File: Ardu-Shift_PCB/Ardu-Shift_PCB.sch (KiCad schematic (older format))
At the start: 16 parts, among them U1 OLED(SPI), U2 Arduino_Pro_Micro

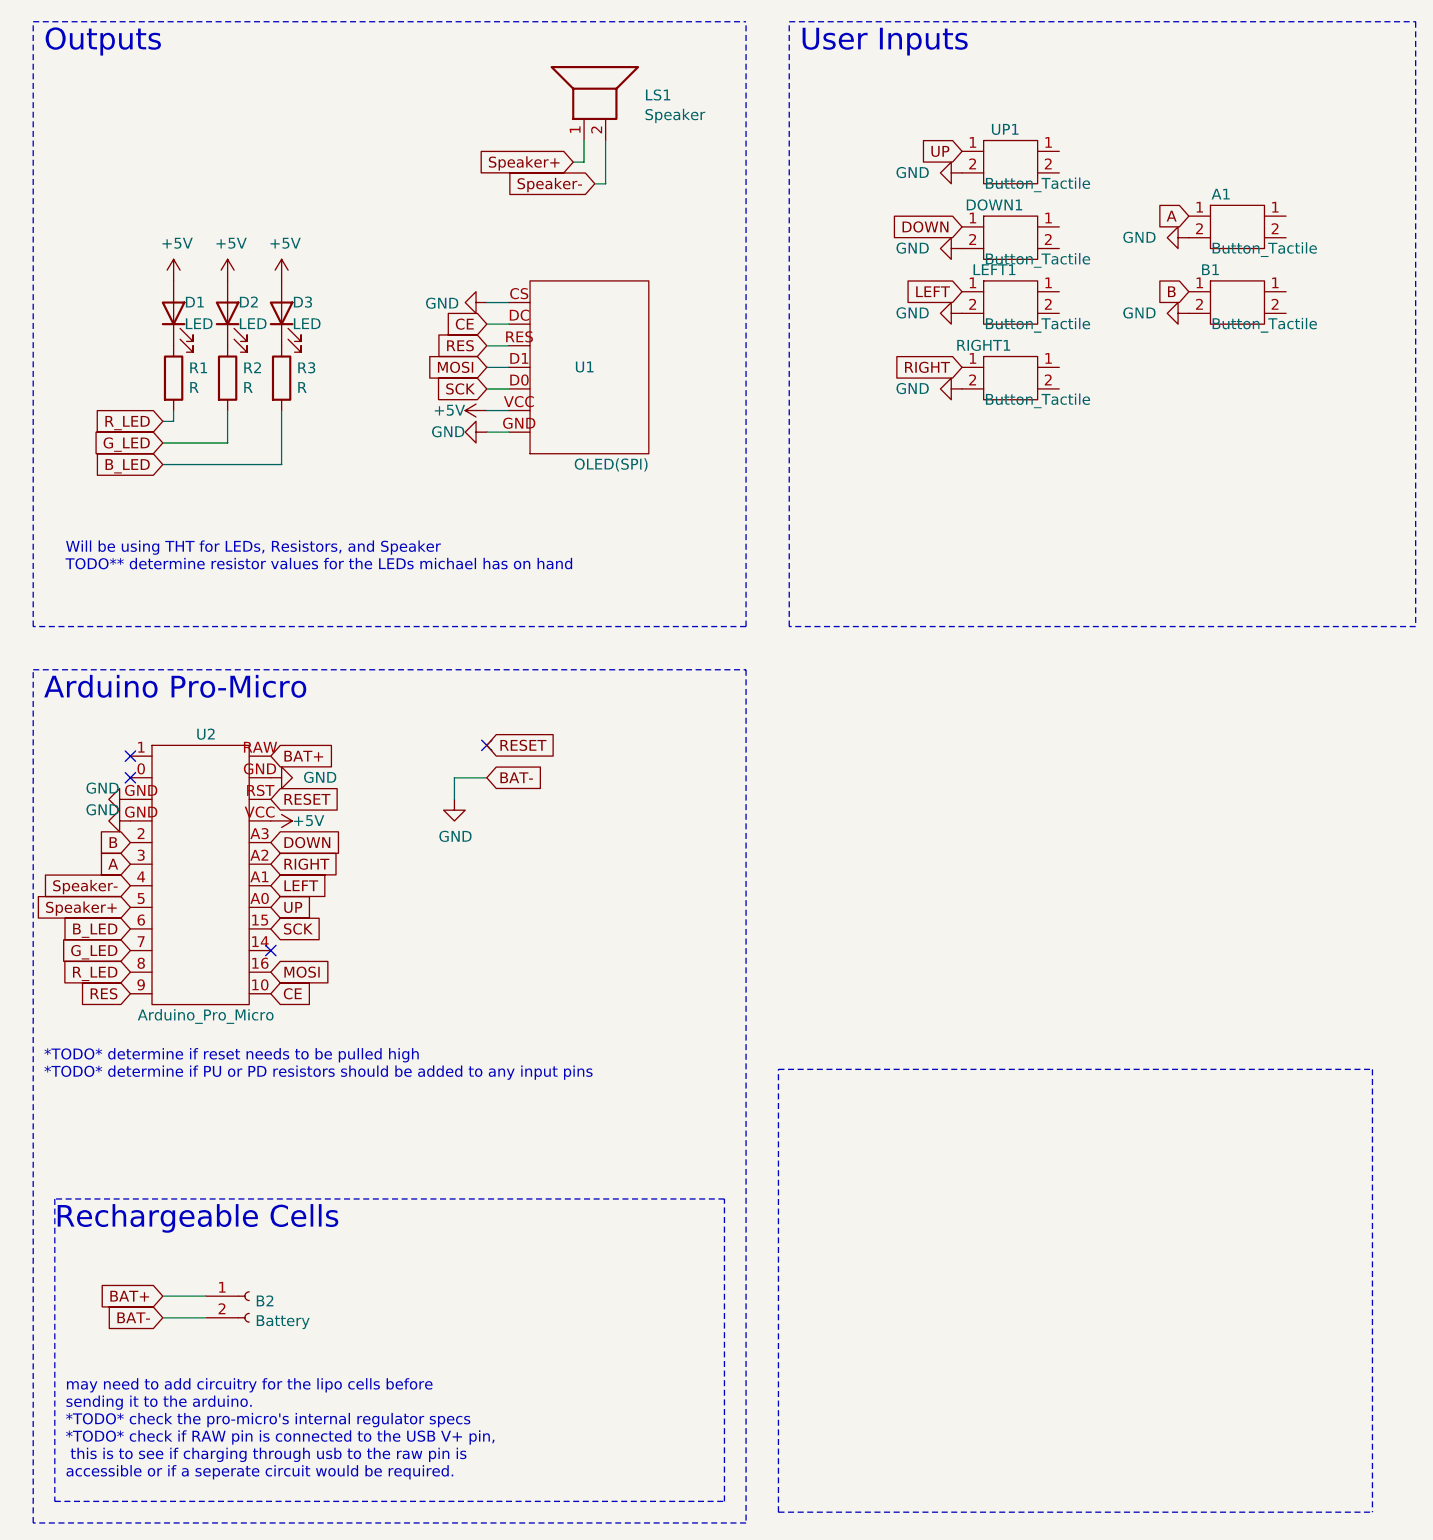
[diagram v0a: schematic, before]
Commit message: first version of the final assembly/routing of game-device PCB
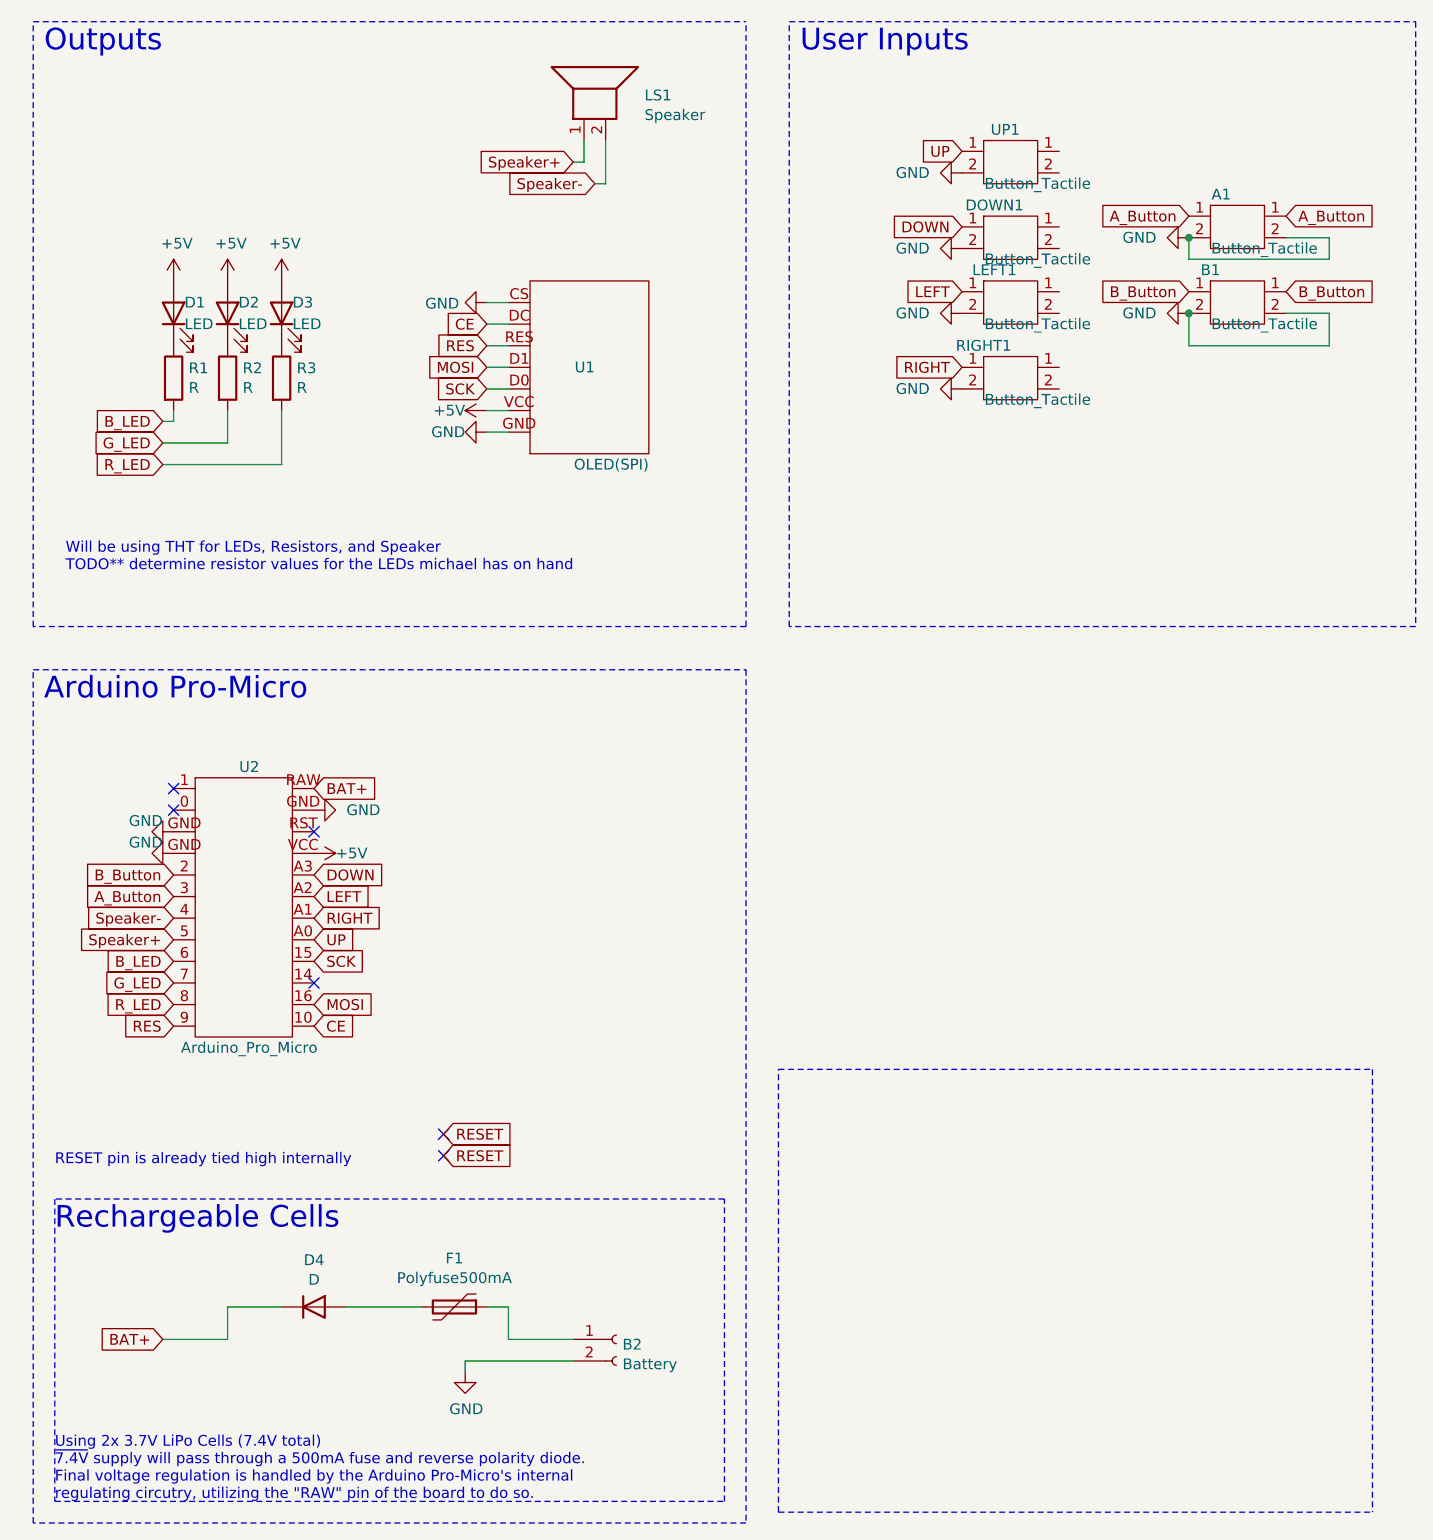
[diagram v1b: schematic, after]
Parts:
- added D4: D, Diode_THT:D_A-405_P10.16mm_Horizontal, symbol Device:D
- added F1: Polyfuse500mA, Resistor_THT:R_Axial_DIN0207_L6.3mm_D2.5mm_P7.62mm_Horizontal, symbol Device:Polyfuse
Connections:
- net A is gone; now on net A_Button: A1.1, U2.3
- net B is gone; now on net B_Button: B1.1, U2.2
- net BAT+: now also D4.1 (K); no longer B2.1 (Pin_1)
- net B_LED: now also R1.2; no longer R3.2
- net LEFT: now also U2.A2; no longer U2.A1
- net RESET: no longer U2.RST
- net RIGHT: now also U2.A1; no longer U2.A2
- net R_LED: now also R3.2; no longer R1.2
- net A_Button: now reaches A1.1
- net B_Button: now reaches B1.1
- new net: B2.1 (Pin_1), F1.1
- new net: D4.2 (A), F1.2
- no-connect marks 4 -> 6
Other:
- note added: "RESET pin is already tied high internally\n"
- note added: "Using 2x 3.7V LiPo Cells (7.4V total)\n~7.4V supply will pass through a 500mA fuse and reverse polarity diode.\nFinal voltage regulation is handled by the Arduino Pro-Micro's internal \nregulating circutry, utilizing the "RAW" pin of the board to do so."
- note removed: "*TODO* determine if reset needs to be pulled high\n*TODO* determine if PU or PD resistors should be added to any input pins"
- note removed: "may need to add circuitry for the lipo cells before \nsending it to the arduino. \n*TODO* check the pro-micro's internal regulator specs\n*TODO* check if RAW pin is connected to the USB V+ pin,\n this is to see if charging through usb to the raw pin is \naccessible or if a seperate circuit would be required.\n"
- moved on the sheet: B2, U2
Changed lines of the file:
@@
 	0    -1   -1   0
 $EndComp
-NoConn ~ 1100 4050
-NoConn ~ 1100 4150
+NoConn ~ 1300 4200
+NoConn ~ 1300 4300
 Text GLabel 3150 1300 0    50   Input ~ 0
 Speaker+
@@
 	1    0    0    -1
 $EndComp
-Text GLabel 1250 2500 0    50   Input ~ 0
+Text GLabel 1250 2700 0    50   Input ~ 0
 R_LED
 Text GLabel 1250 2600 0    50   Input ~ 0
 G_LED
-Text GLabel 1250 2700 0    50   Input ~ 0
+Text GLabel 1250 2500 0    50   Input ~ 0
 B_LED
 Wire Wire Line
@@
 Wire Wire Line
 	1250 2700 1800 2700
-Text GLabel 1100 5050 0    50   Input ~ 0
+Text GLabel 1300 5200 0    50   Input ~ 0
 R_LED
-Text GLabel 1100 4950 0    50   Input ~ 0
+Text GLabel 1300 5100 0    50   Input ~ 0
 G_LED
 $Comp
 L power:GND #PWR0104
 U 1 1 602F2938
-P 1100 4250
-F 0 "#PWR0104" H 1100 4000 50  0001 C CNN
-F 1 "GND" V 1050 4200 50  0000 R CNN
-F 2 "" H 1100 4250 50  0001 C CNN
-F 3 "" H 1100 4250 50  0001 C CNN
-	1    1100 4250
+P 1300 4400
+F 0 "#PWR0104" H 1300 4150 50  0001 C CNN
+F 1 "GND" V 1250 4350 50  0000 R CNN
+F 2 "" H 1300 4400 50  0001 C CNN
+F 3 "" H 1300 4400 50  0001 C CNN
+	1    1300 4400
 	0    1    1    0
 $EndComp
@@
 L power:GND #PWR0106
 U 1 1 602F760D
-P 1750 4150
-F 0 "#PWR0106" H 1750 3900 50  0001 C CNN
-F 1 "GND" V 1750 4000 50  0000 R CNN
-F 2 "" H 1750 4150 50  0001 C CNN
-F 3 "" H 1750 4150 50  0001 C CNN
-	1    1750 4150
+P 1950 4300
+F 0 "#PWR0106" H 1950 4050 50  0001 C CNN
+F 1 "GND" V 1950 4150 50  0000 R CNN
+F 2 "" H 1950 4300 50  0001 C CNN
+F 3 "" H 1950 4300 50  0001 C CNN
+	1    1950 4300
 	0    -1   -1   0
 $EndComp
 Text GLabel 2750 2250 0    50   Input ~ 0
 MOSI
-Text GLabel 1750 5050 2    50   Input ~ 0
+Text GLabel 1950 5200 2    50   Input ~ 0
 MOSI
 Text GLabel 2750 2050 0    50   Input ~ 0
 CE
-Text GLabel 1750 5150 2    50   Input ~ 0
+Text GLabel 1950 5300 2    50   Input ~ 0
 CE
 $Comp
@@
 Text GLabel 2750 2150 0    50   Input ~ 0
 RES
-Text GLabel 1100 5150 0    50   Input ~ 0
+Text GLabel 1300 5300 0    50   Input ~ 0
 RES
-Text GLabel 1750 4250 2    50   Input ~ 0
+Text GLabel 2550 5900 2    50   Input ~ 0
 RESET
-Text GLabel 1100 4850 0    50   Input ~ 0
+Text GLabel 1300 5000 0    50   Input ~ 0
 B_LED
-Text GLabel 1750 4750 2    50   Input ~ 0
+Text GLabel 1950 4900 2    50   Input ~ 0
 UP
-Text GLabel 1750 4450 2    50   Input ~ 0
+Text GLabel 1950 4600 2    50   Input ~ 0
 DOWN
-Text GLabel 1750 4550 2    50   Input ~ 0
+Text GLabel 1950 4800 2    50   Input ~ 0
 RIGHT
-Text GLabel 1750 4650 2    50   Input ~ 0
+Text GLabel 1950 4700 2    50   Input ~ 0
 LEFT
-Text GLabel 1750 4850 2    50   Input ~ 0
+Text GLabel 1950 5000 2    50   Input ~ 0
 SCK
 Text GLabel 2750 2350 0    50   Input ~ 0
 SCK
-NoConn ~ 1750 4950
+NoConn ~ 1950 5100
 $Comp
 L power:GND #PWR0109
@@
 $EndComp
 Text GLabel 6000 1900 0    50   Input ~ 0
-B
+B_Button
 Text GLabel 6000 1550 0    50   Input ~ 0
-A
+A_Button
 $Comp
 L Device:Button_Tactile B1
@@
 	1    0    0    -1
 $EndComp
-Text GLabel 2750 4000 2    50   Input ~ 0
+Text GLabel 2550 5800 2    50   Input ~ 0
 RESET
 Wire Notes Line
@@
 Text Notes 4200 800  0    100  ~ 0
 User Inputs\n
-Text GLabel 1250 6550 0    50   Input ~ 0
+Text GLabel 1250 6750 0    50   Input ~ 0
 BAT+
 Wire Notes Line
@@
 Text Notes 750  6250 0    100  ~ 0
 Rechargeable Cells\n
-Text GLabel 1750 4050 2    50   Input ~ 0
+Text GLabel 1950 4200 2    50   Input ~ 0
 BAT+
 Wire Notes Line
@@
 Wire Notes Line
 	3850 6100 750  6100
-Text GLabel 1250 6650 0    50   Input ~ 0
-BAT-
-Text GLabel 2750 4150 2    50   Input ~ 0
-BAT-
 $Comp
 L Connector:Conn_01x02_Female B2
 U 1 1 603C890C
-P 1650 6550
-F 0 "B2" H 1678 6526 50  0000 L CNN
-F 1 "Battery" H 1678 6435 50  0000 L CNN
-F 2 "Connector_PinHeader_2.54mm:PinHeader_1x02_P2.54mm_Vertical" H 1650 6550 50  0001 C CNN
-F 3 "~" H 1650 6550 50  0001 C CNN
-	1    1650 6550
-	1    0    0    -1
-$EndComp
-Wire Wire Line
-	1250 6650 1450 6650
-Wire Wire Line
-	1250 6550 1450 6550
-$Comp
-L power:GND #PWR0116
-U 1 1 603CB5E7
-P 2600 4250
-F 0 "#PWR0116" H 2600 4000 50  0001 C CNN
-F 1 "GND" H 2605 4077 50  0000 C CNN
-F 2 "" H 2600 4250 50  0001 C CNN
-F 3 "" H 2600 4250 50  0001 C CNN
-	1    2600 4250
-	1    0    0    -1
-$EndComp
-Wire Wire Line
-	2600 4250 2600 4150
-Wire Wire Line
-	2600 4150 2750 4150
-NoConn ~ 2750 4000
+P 3350 6750
+F 0 "B2" H 3378 6726 50  0000 L CNN
+F 1 "Battery" H 3378 6635 50  0000 L CNN
+F 2 "Connector_PinHeader_2.54mm:PinHeader_1x02_P2.54mm_Vertical" H 3350 6750 50  0001 C CNN
+F 3 "~" H 3350 6750 50  0001 C CNN
+	1    3350 6750
+	1    0    0    -1
+$EndComp
+NoConn ~ 2550 5800
 $Comp
 L power:GND #PWR0117
 U 1 1 603CE810
-P 1100 4350
-F 0 "#PWR0117" H 1100 4100 50  0001 C CNN
-F 1 "GND" V 1050 4300 50  0000 R CNN
-F 2 "" H 1100 4350 50  0001 C CNN
-F 3 "" H 1100 4350 50  0001 C CNN
-	1    1100 4350
+P 1300 4500
+F 0 "#PWR0117" H 1300 4250 50  0001 C CNN
+F 1 "GND" V 1250 4450 50  0000 R CNN
+F 2 "" H 1300 4500 50  0001 C CNN
+F 3 "" H 1300 4500 50  0001 C CNN
+	1    1300 4500
 	0    1    1    0
 $EndComp
@@
 Wire Notes Line
 	3950 3650 3950 7600
-Text Notes 800  7400 0    50   ~ 0
-may need to add circuitry for the lipo cells before \nsending it to the arduino. \n*TODO* check the pro-micro's internal regulator specs\n*TODO* check if RAW pin is connected to the USB V+ pin,\n this is to see if charging through usb to the raw pin is \naccessible or if a seperate circuit would be required.\n
+Text Notes 750  7500 0    50   ~ 0
+Using 2x 3.7V LiPo Cells (7.4V total)\n~7.4V supply will pass through a 500mA fuse and reverse polarity diode.\nFinal voltage regulation is handled by the Arduino Pro-Micro's internal \nregulating circutry, utilizing the "RAW" pin of the board to do so.
 Text Notes 800  3200 0    50   ~ 0
 Will be using THT for LEDs, Resistors, and Speaker \nTODO** determine resistor values for the LEDs michael has on hand\n
-Text Notes 700  5550 0    50   ~ 0
-*TODO* determine if reset needs to be pulled high\n*TODO* determine if PU or PD resistors should be added to any input pins
-Text GLabel 1100 4450 0    50   Input ~ 0
-B
-Text GLabel 1100 4550 0    50   Input ~ 0
-A
+Text Notes 750  5950 0    50   ~ 0
+RESET pin is already tied high internally\n
+Text GLabel 1300 4600 0    50   Input ~ 0
+B_Button
+Text GLabel 1300 4700 0    50   Input ~ 0
+A_Button
 $Comp
 L power:+5V #PWR0105
 U 1 1 602F42C8
-P 1750 4350
-F 0 "#PWR0105" H 1750 4200 50  0001 C CNN
-F 1 "+5V" V 1750 4450 50  0000 L CNN
-F 2 "" H 1750 4350 50  0001 C CNN
-F 3 "" H 1750 4350 50  0001 C CNN
-	1    1750 4350
-	0    1    1    0
-$EndComp
-Text GLabel 1100 4650 0    50   Input ~ 0
+P 1950 4500
+F 0 "#PWR0105" H 1950 4350 50  0001 C CNN
+F 1 "+5V" V 1950 4600 50  0000 L CNN
+F 2 "" H 1950 4500 50  0001 C CNN
+F 3 "" H 1950 4500 50  0001 C CNN
+	1    1950 4500
+	0    1    1    0
+$EndComp
+Text GLabel 1300 4800 0    50   Input ~ 0
 Speaker-
-Text GLabel 1100 4750 0    50   Input ~ 0
+Text GLabel 1300 4900 0    50   Input ~ 0
 Speaker+
 $Comp
 L Device:Arduino_Pro_Micro U2
 U 1 1 602C193C
-P 1450 4050
-F 0 "U2" H 1450 4150 50  0000 C CNN
-F 1 "Arduino_Pro_Micro" H 1450 2850 50  0000 C CNN
-F 2 "Module:Arduino_Pro_Micro" H 450 3500 50  0001 C CNN
-F 3 "" H 450 3500 50  0001 C CNN
-	1    1450 4050
-	1    0    0    -1
-$EndComp
+P 1650 4200
+F 0 "U2" H 1650 4300 50  0000 C CNN
+F 1 "Arduino_Pro_Micro" H 1650 3000 50  0000 C CNN
+F 2 "Module:Arduino_Pro_Micro" H 650 3650 50  0001 C CNN
+F 3 "" H 650 3650 50  0001 C CNN
+	1    1650 4200
+	1    0    0    -1
+$EndComp
+$Comp
+L Device:Polyfuse F1
+U 1 1 6044FB48
+P 2600 6600
+F 0 "F1" V 2375 6600 50  0000 C CNN
+F 1 "Polyfuse500mA" V 2466 6600 50  0000 C CNN
+F 2 "Resistor_THT:R_Axial_DIN0207_L6.3mm_D2.5mm_P7.62mm_Horizontal" H 2650 6400 50  0001 L CNN
+F 3 "~" H 2600 6600 50  0001 C CNN
+	1    2600 6600
+	0    1    1    0
+$EndComp
+Wire Wire Line
+	2750 6600 2850 6600
+Wire Wire Line
+	2850 6600 2850 6750
+Wire Wire Line
+	2850 6750 3150 6750
+$Comp
+L Device:D D4
+U 1 1 604552AC
+P 1950 6600
+F 0 "D4" H 1950 6817 50  0000 C CNN
+F 1 "D" H 1950 6726 50  0000 C CNN
+F 2 "Diode_THT:D_A-405_P10.16mm_Horizontal" H 1950 6600 50  0001 C CNN
+F 3 "~" H 1950 6600 50  0001 C CNN
+	1    1950 6600
+	1    0    0    -1
+$EndComp
+Wire Wire Line
+	1800 6600 1550 6600
+Wire Wire Line
+	1550 6600 1550 6750
+Wire Wire Line
+	1250 6750 1550 6750
+Wire Wire Line
+	2100 6600 2450 6600
+NoConn ~ 2550 5900
+NoConn ~ 1950 4400
+$Comp
+L power:GND #PWR0116
+U 1 1 6048AF00
+P 2650 6900
+F 0 "#PWR0116" H 2650 6650 50  0001 C CNN
+F 1 "GND" H 2655 6727 50  0000 C CNN
+F 2 "" H 2650 6900 50  0001 C CNN
+F 3 "" H 2650 6900 50  0001 C CNN
+	1    2650 6900
+	1    0    0    -1
+$EndComp
+Wire Wire Line
+	2650 6900 2650 6850
+Wire Wire Line
+	2650 6850 3150 6850
+Text GLabel 6450 1550 2    50   Input ~ 0
+A_Button
+Text GLabel 6450 1900 2    50   Input ~ 0
+B_Button
+Wire Wire Line
+	6450 2000 6650 2000
+Wire Wire Line
+	6650 2000 6650 2150
+Wire Wire Line
+	6650 2150 6000 2150
+Wire Wire Line
+	6000 2150 6000 2000
+Connection ~ 6000 2000
+Wire Wire Line
+	6450 1650 6650 1650
+Wire Wire Line
+	6650 1650 6650 1750
+Wire Wire Line
+	6650 1750 6000 1750
+Wire Wire Line
+	6000 1750 6000 1650
+Connection ~ 6000 1650
 $EndSCHEMATC
